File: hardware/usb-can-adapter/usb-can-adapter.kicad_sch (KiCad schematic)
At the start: 11 parts

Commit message: feat(adapter): add LEDs, SWD header and USB-C
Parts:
- added D1: RED, symbol Device:LED
- added D2: BLUE, symbol Device:LED
- added D3: GREEN, symbol Device:LED
- added J1: SWD, symbol Connector_Generic:Conn_01x05
- added J2: USB_C_Receptacle_USB2.0_16P, symbol Connector:USB_C_Receptacle_USB2.0_16P
- added R1, R2, R3: 1K, symbol Device:R
- added R4, R5: 5.1k, symbol Device:R
- gave numbers to parts that had none: 10
- renumbered C to C5
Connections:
- net +3V3: now also J1.1 (Pin_1), R1.1, R2.1, R3.1
- net GND: now also D1.1 (K), J1.5 (Pin_5), J2.A1 (GND), J2.A12 (GND), J2.B1 (GND), J2.B12 (GND), J2.SH (SHIELD), R4.2, R5.2
- net NRST: now also J1.4 (Pin_4)
- net SWCLK: now also J1.3 (Pin_3)
- net SWDIO: now also J1.2 (Pin_2)
- net USB_DM: now also J2.A7 (D-), J2.B7 (D-)
- net USB_DP: now also J2.A6 (D+), J2.B6 (D+)
- net LED_GREEN: now reaches U1.25 (PB11)
- net LED_GREEN: now also D3.1 (K)
- net LED_BLUE: now reaches U1.39 (PA15)
- net LED_BLUE: now also D2.1 (K)
- new net: D3.2 (A), R3.2
- new net: D2.2 (A), R2.2
- new net: D1.2 (A), R1.2
- new net CC1: J2.A5 (CC1), R4.1
- new net CC2: J2.B5 (CC2), R5.1
- new net VBUS: J2.A4 (VBUS), J2.A9 (VBUS), J2.B4 (VBUS), J2.B9 (VBUS)
- no-connect marks 0 -> 2

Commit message: feat(adapter): add LDO, USB ESD and 24 MHz crystal
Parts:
- added C11, C12: 1uF, symbol Device:C
- added C13, C14: 15pF, symbol Device:C
- added U2: AP2112K-3.3, Package_TO_SOT_SMD:SOT-23-5, symbol Regulator_Linear:AP2112K-3.3
- added U3: USBLC6-2SC6, Package_TO_SOT_SMD:SOT-23-6, symbol Power_Protection:USBLC6-2SC6
- added Y1: 24MHz, Crystal:Crystal_SMD_3225-4Pin_3.2x2.5mm, symbol Device:Crystal_GND24
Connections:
- net +3V3: now also C11.1, U2.5 (VOUT)
- net GND: now also C11.2, C12.2, C13.2, C14.2, U2.2 (GND), U3.2 (GND), Y1.2 (G), Y1.4 (G)
- net USB_DM: now also U3.3 (I/O2), U3.4 (I/O2)
- net USB_DP: now also U3.1 (I/O1), U3.6 (I/O1)
- net VBUS: now also C12.1, U2.1 (VIN), U2.3 (EN), U3.5 (VBUS)
- net OSC_IN: now reaches U1.5 (PF0)
- net OSC_IN: now also C13.1, Y1.1
- net OSC_OUT: now reaches U1.6 (PF1)
- net OSC_OUT: now also C14.1, Y1.3

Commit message: feat(adapter): add CAN transceiver and ESD
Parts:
- added C15: 100nF, symbol Device:C
- added D4: NUP2105L, Package_TO_SOT_SMD:SOT-23, symbol Power_Protection:NUP2105L
- added J3: Conn_01x03, symbol Connector_Generic:Conn_01x03
- added J4: Conn_01x02, symbol Connector_Generic:Conn_01x02
- added R6: 120, symbol Device:R
- added U4: SN65HVD230, Package_SO:SOIC-8_3.9x4.9mm_P1.27mm, symbol Interface_CAN_LIN:SN65HVD230
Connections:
- net +3V3: now also C15.1, U4.3 (VCC)
- net CAN_RX: now also U4.4 (R)
- net CAN_TX: now also U4.1 (D)
- net GND: now also C15.2, D4.3 (A), J3.3 (Pin_3), U4.2 (GND)
- net CAN_STBY: now reaches U1.8 (PA0)
- net CAN_STBY: now also U4.8 (Rs)
- new net: J4.1 (Pin_1), R6.2
- new net CAN_H: D4.1 (K), J3.1 (Pin_1), R6.1, U4.7 (CANH)
- new net CAN_L: D4.2 (K), J3.2 (Pin_2), J4.2 (Pin_2), U4.6 (CANL)
- no-connect marks 2 -> 3

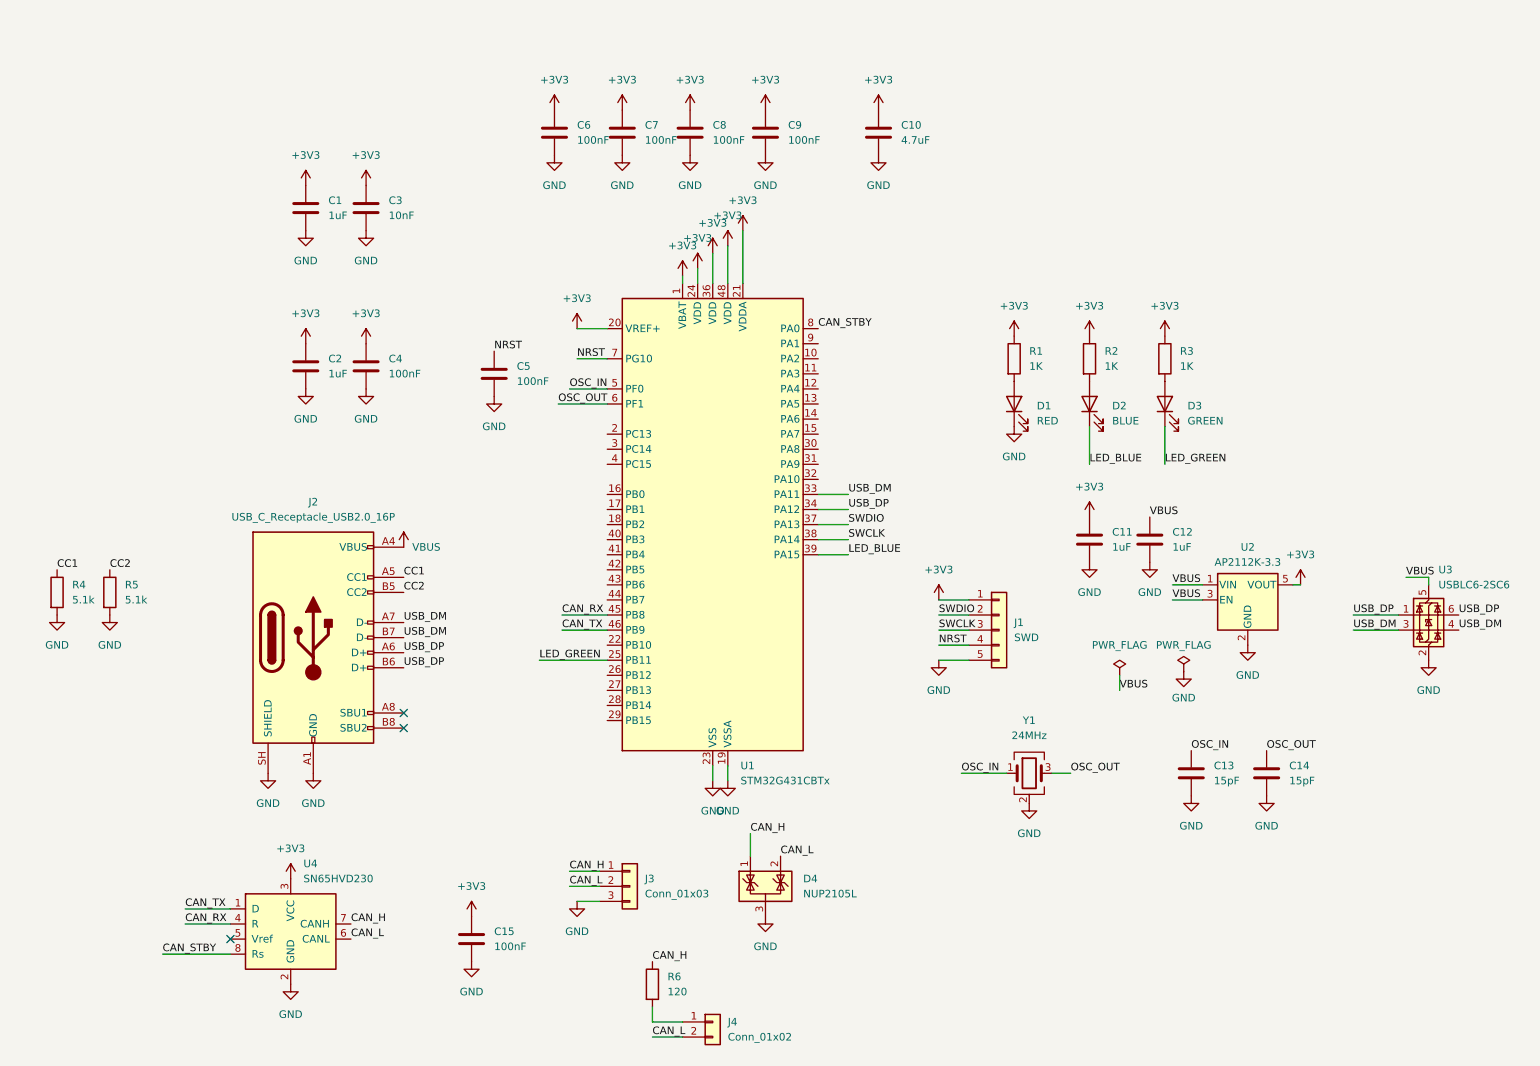
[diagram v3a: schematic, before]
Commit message: feat(adapter): add BOOT0 and switched CAN power
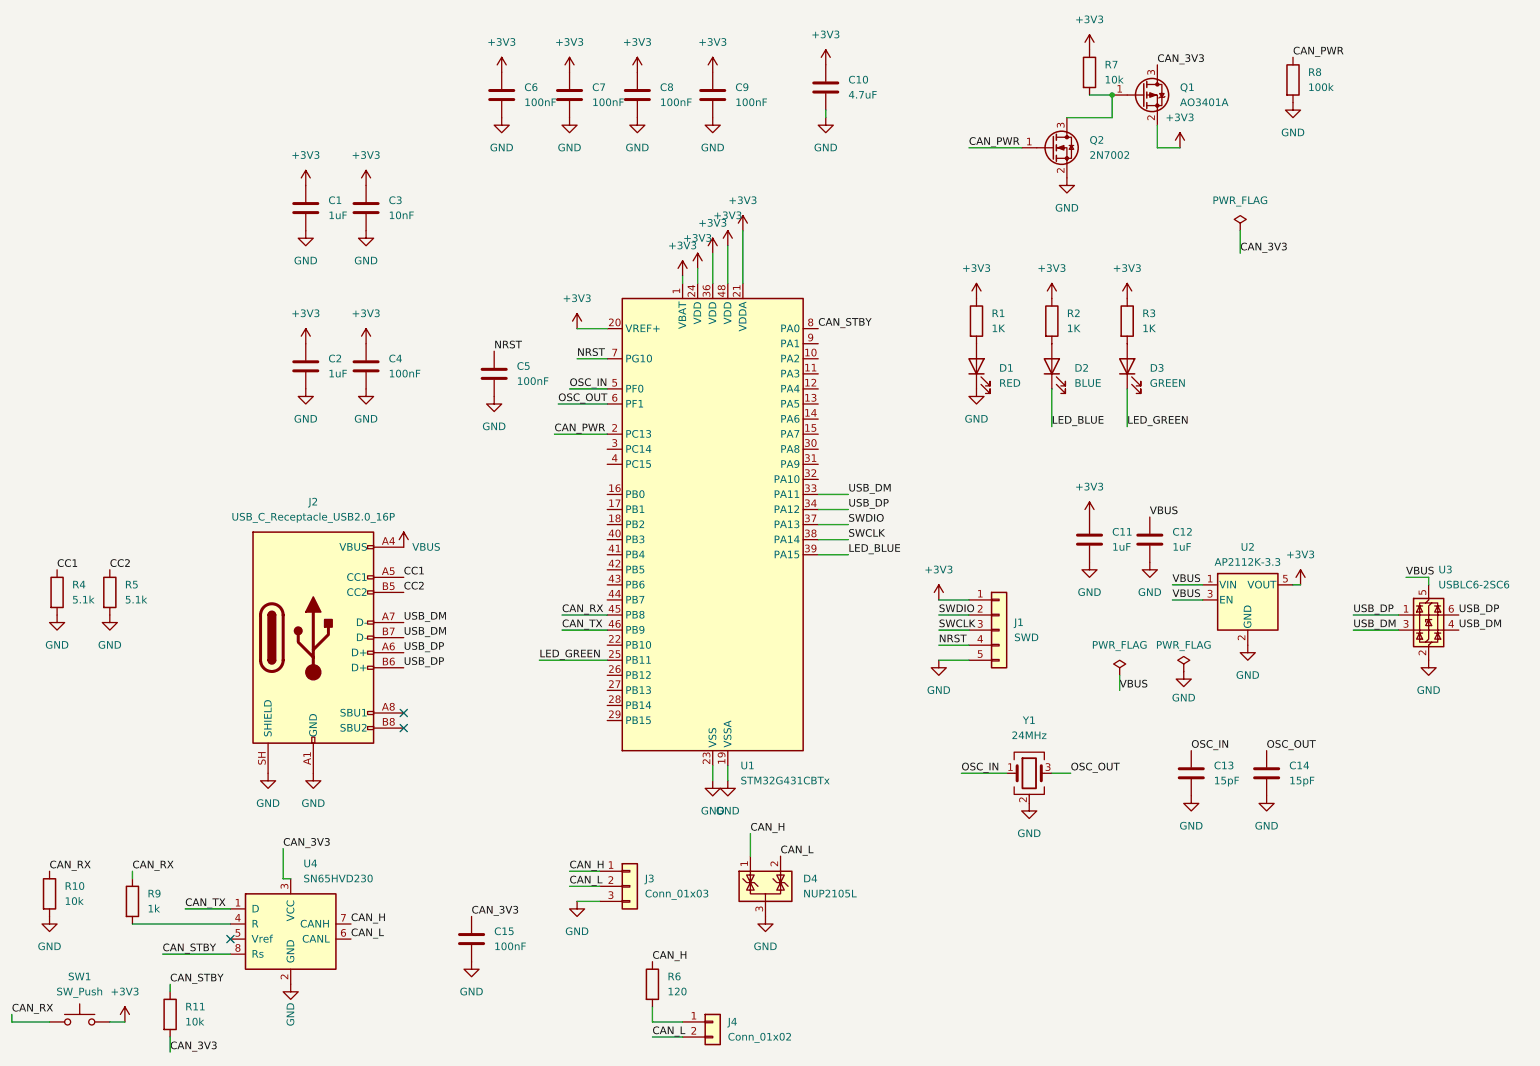
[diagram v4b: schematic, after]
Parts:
- added Q1: AO3401A, Package_TO_SOT_SMD:SOT-23, symbol Transistor_FET:AO3401A
- added Q2: 2N7002, Package_TO_SOT_SMD:SOT-23, symbol Transistor_FET:2N7002
- added R10, R11, R7: 10k, symbol Device:R
- added R8: 100k, symbol Device:R
- added R9: 1k, symbol Device:R
- added SW1: SW_Push, symbol Switch:SW_Push
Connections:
- net +3V3: now also Q1.2 (S), R7.1, SW1.2; no longer C15.1, U4.3 (VCC)
- net CAN_RX: now also R10.1, R9.1, SW1.1; no longer U4.4 (R)
- net CAN_STBY: now also R11.1
- net GND: now also Q2.2 (S), R10.2, R8.2
- net CAN_PWR: now reaches U1.2 (PC13)
- net CAN_PWR: now also Q2.1 (G), R8.1
- new net: Q1.1 (G), Q2.3 (D), R7.2
- new net: R9.2, U4.4 (R)
- new net CAN_3V3: C15.1, Q1.3 (D), R11.2, U4.3 (VCC)
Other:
- moved on the sheet: C10, C6, C7, C8, C9, D1, D2, D3, R1, R2, R3
